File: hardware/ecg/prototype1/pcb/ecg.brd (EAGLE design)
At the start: 100 x 80 mm, 21 parts

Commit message: no comment
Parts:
- removed C5: 10uF, adafruit:C0805
- removed LED3: (no value), adafruit:LED3MM
- removed R3: (no value), resistor:R0805
- added C6, C7: 1uF, adafruit:C0805
- moved JP1 36.9 mm to (29.2, 8.89)
- moved LED1 5.32 mm to (72.4, 46.7)
- moved R1 5.32 mm to (67.3, 46.7), turned to 180 degrees
- moved LED2 5.09 mm to (72.4, 41.6)
- moved R2 5.09 mm to (67.3, 41.6), turned to 180 degrees
- moved U$4 5.08 mm to (10.2, 14.0)
- moved U$3 4.02 mm to (29.2, 43.2), turned to 270 degrees
- moved C3 4.02 mm to (26.7, 35.6), turned to 0 degrees
- moved JP2 2.54 mm to (53.3, 45.7)
- moved JP4 2.54 mm to (14.0, 45.7)
- moved C2 1.27 mm to (11.4, 30.5)
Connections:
- removed net N$28: C3.2, U$1.P$24
- removed net N$31: LED3.A, R3.1
- new net N$27: C6.1, U$1.P$11
- new net N$32: C7.1, U$1.P$27
- new net ULED1: R1.2, U$1.P$26
- new net ULED2: R2.2, U$2.28
- net GND: now also C3.2, C6.2, C7.2, U$1.P$24; no longer C5.2, LED3.K
- net VDD: now also JP5.1; no longer C5.1
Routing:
- net N$18: track 85.9 -> 21.6 mm
- net ULED1: track 0.00 -> 57.6 mm
- net N$19: track 58.6 -> 14.5 mm, vias 1 -> 0
- net ULED2: track 0.00 -> 18.2 mm
- net N$20: track 43.6 -> 26.5 mm, vias 0 -> 1
- net N$25: track 37.9 -> 22.2 mm, vias 1 -> 0
- net N$6: track 65.9 -> 77.7 mm, vias 1 -> 0
- net N$16: track 25.7 -> 15.2 mm
- net N$22: track 102.9 -> 93.0 mm
- net VDD: track 153.6 -> 144.6 mm, vias 2 -> 1
- net N$26: track 35.7 -> 27.1 mm
- net N$31: track 8.22 -> 0.00 mm
- net N$17: track 16.8 -> 24.8 mm, vias 0 -> 1
- net N$24: track 32.1 -> 24.4 mm, vias 1 -> 0
- net N$23: track 93.5 -> 86.2 mm, vias 1 -> 0
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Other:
- board size 100 x 80 mm -> 81 x 50.8 mm

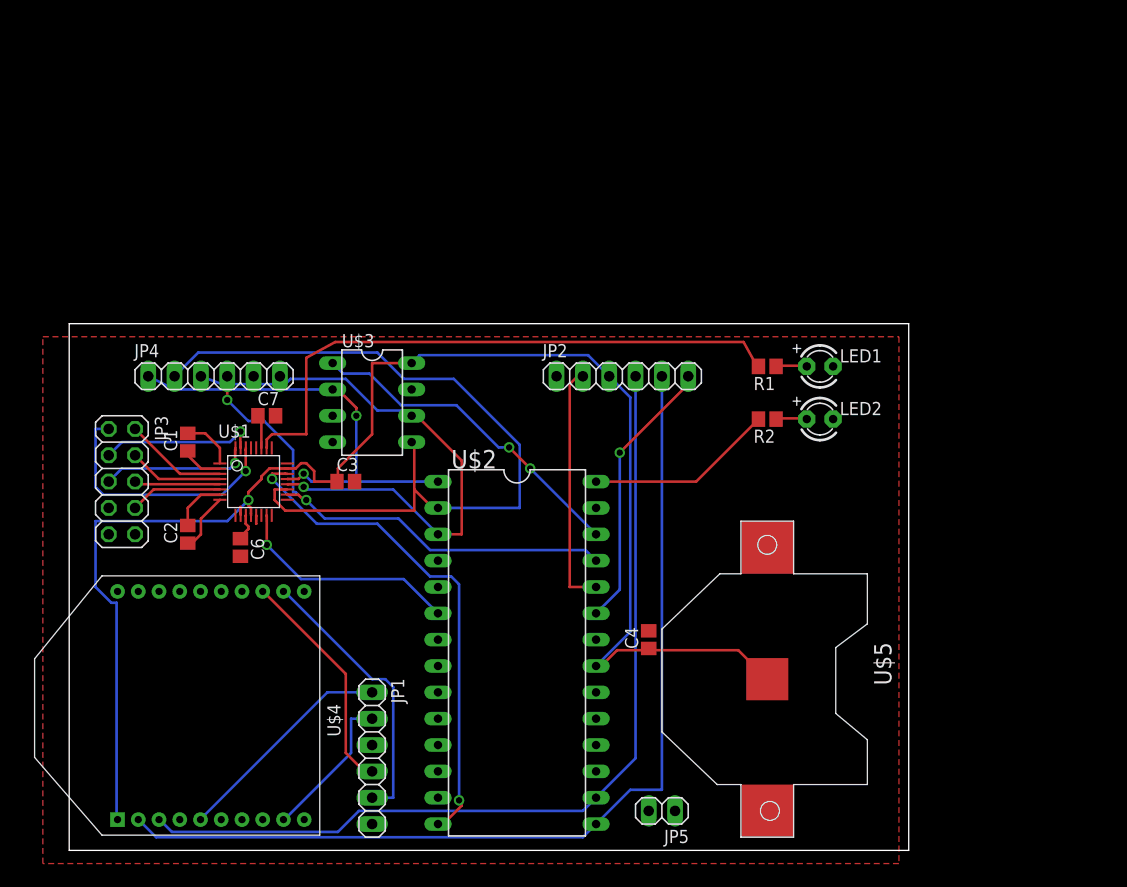
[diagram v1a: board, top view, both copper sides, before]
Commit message: PCB v0.1.2, sent to EuroCircuits for fab.
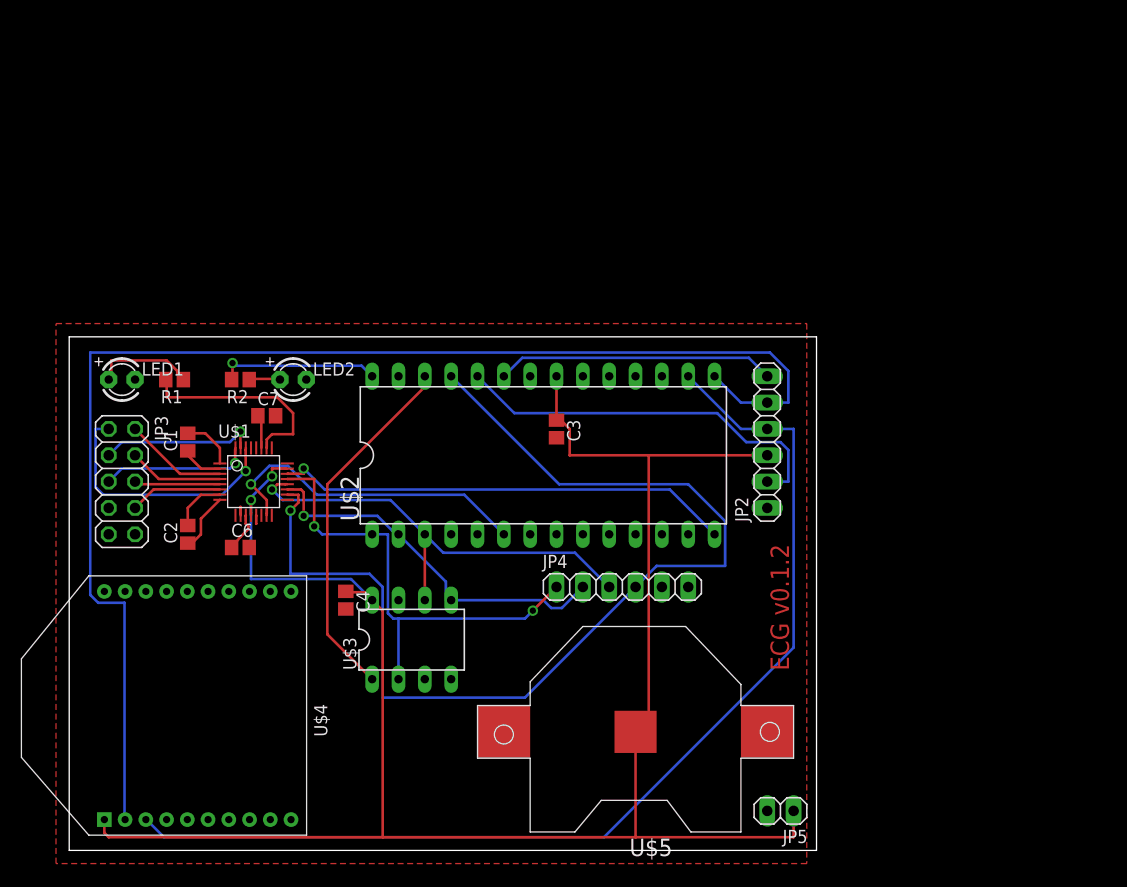
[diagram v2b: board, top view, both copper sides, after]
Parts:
- removed JP1: (no value), pinhead:1X06
- moved LED1 67.3 mm to (5.08, 45.4)
- moved R1 57.2 mm to (10.2, 45.4)
- moved LED2 50.9 mm to (21.6, 45.4)
- moved R2 50.9 mm to (16.5, 45.4)
- moved JP4 44.3 mm to (53.3, 25.4)
- moved C4 29.5 mm to (26.7, 24.1), turned to 270 degrees
- moved U$3 23.2 mm to (33.0, 20.3), turned to 0 degrees
- moved C3 20.9 mm to (47.0, 40.6), turned to 270 degrees
- moved U$2 19.2 mm to (45.7, 38.1), turned to 0 degrees
- moved JP2 15.3 mm to (67.3, 39.4), turned to 90 degrees
- moved U$5 13.7 mm to (54.6, 11.4), turned to 180 degrees
- moved JP5 11.4 mm to (68.6, 3.81)
- moved U$4 1.27 mm to (8.89, 14.0)
- turned C6 to 0 degrees
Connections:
- removed net N$18: JP1.1, U$4.5
- removed net N$19: JP1.2, U$4.9
- removed net N$25: JP1.4, U$4.13
- removed net N$26: JP1.5, U$4.12
- new net N$28: U$4.5
- new net N$31: U$4.9
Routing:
- net N$8: track 48.7 -> 103.9 mm, vias 2 -> 1
- net VDD: track 144.6 -> 189.2 mm, vias 1 -> 2
- net N$6: track 77.7 -> 36.6 mm, vias 0 -> 1
- net ULED1: track 57.6 -> 20.2 mm
- net N$22: track 93.0 -> 127.2 mm
- net N$26: track 27.1 -> 0.00 mm
- net N$25: track 22.2 -> 0.00 mm
- net N$18: track 21.6 -> 0.00 mm
- net N$23: track 86.2 -> 104.1 mm
- net N$19: track 14.5 -> 0.00 mm
- net N$24: track 24.4 -> 38.0 mm
- net N$7: track 54.8 -> 44.4 mm
- net N$14: track 22.1 -> 31.5 mm
- net N$29: track 3.04 -> 9.80 mm
- net N$9: track 48.7 -> 44.3 mm, vias 2 -> 1
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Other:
- board size 81 x 50.8 mm -> 72.1 x 49.5 mm
- board text added: "ECG v0.1.2"
